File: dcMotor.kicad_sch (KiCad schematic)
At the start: 132 parts, among them J1 USB_C_Receptacle_USB2.0_16P, J3 Conn_ST_STDC14, J6 Conn_01x02_Pin, J7 Conn_01x04_Pin, J8 Conn_01x06_Pin, Q1 AO3400A, SW1 SW_Push, SW2 SW_Push, U1 LMR54406DBVR, U10 MCP6561-OT, U11 TLV9152IDR, U12 NUCLEO-F411RE:NUCLEO-F411RE, U2 NCP718ASNADJT1G, U3 NCP718ASNADJT1G, U5 TLV9152IDR, U6 ER_OLEDM0.91_1x-I2C, U7 STM32G431CBTx, U8 LTH-301-05, U9 DRV8231ADDA

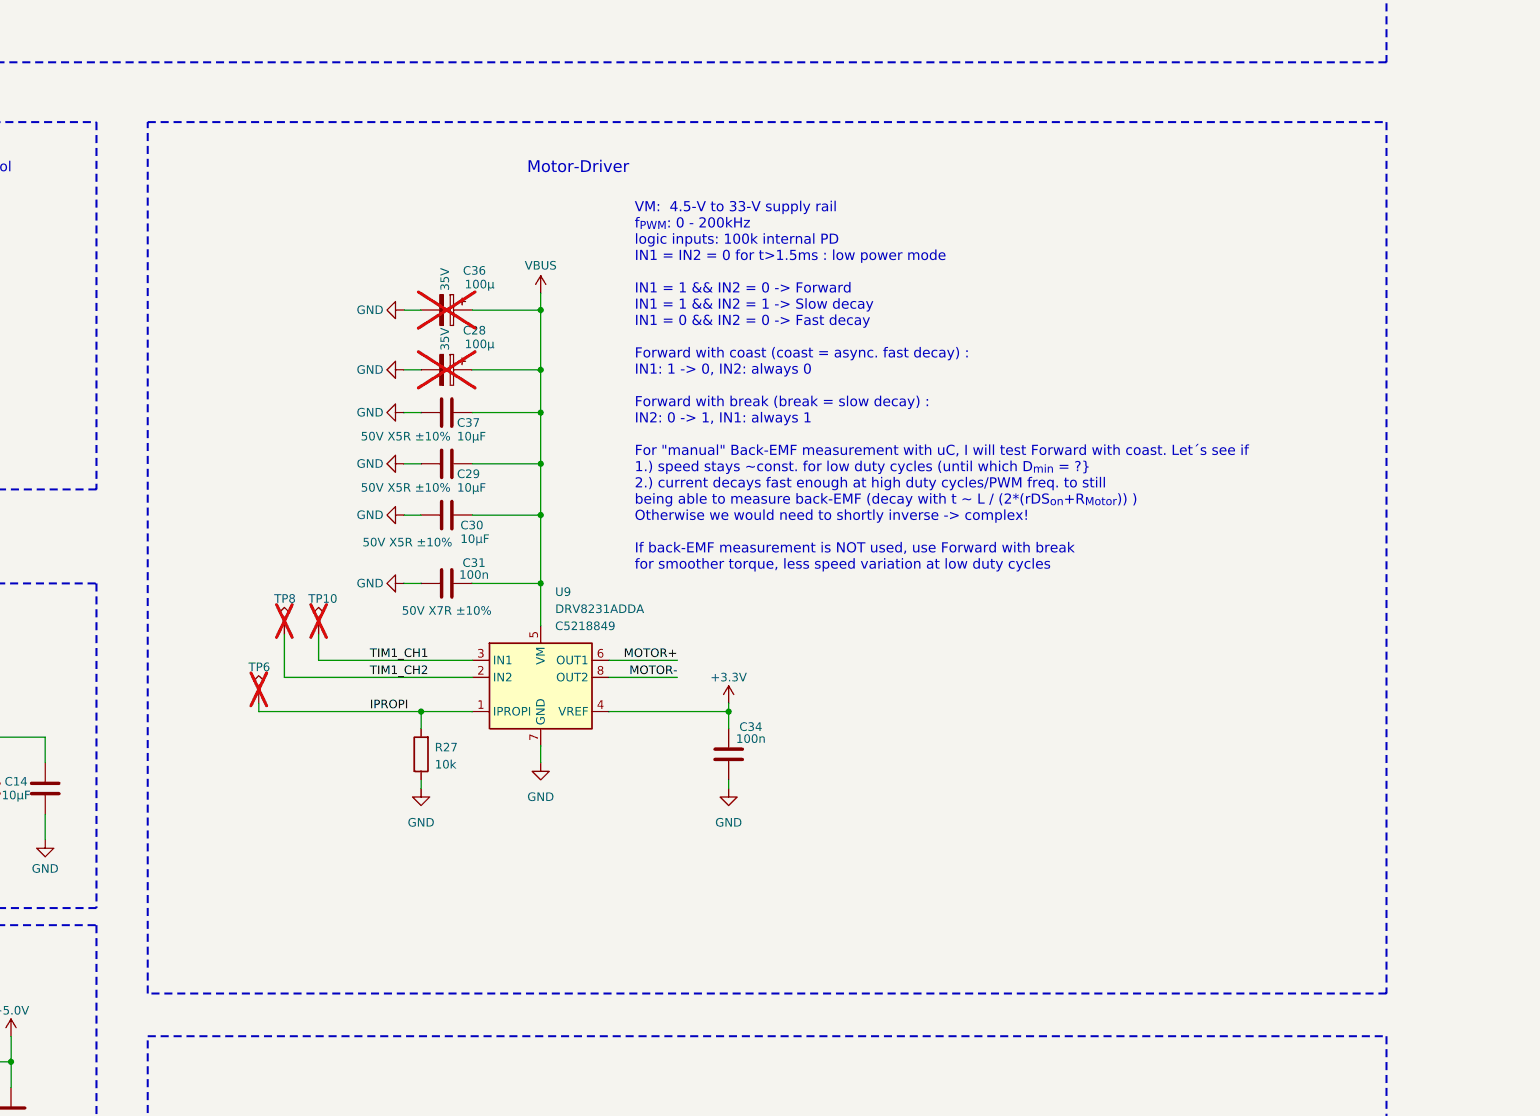
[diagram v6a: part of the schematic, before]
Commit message: added filter caps on pwm inputs because of DRV8321 errata (glitches)
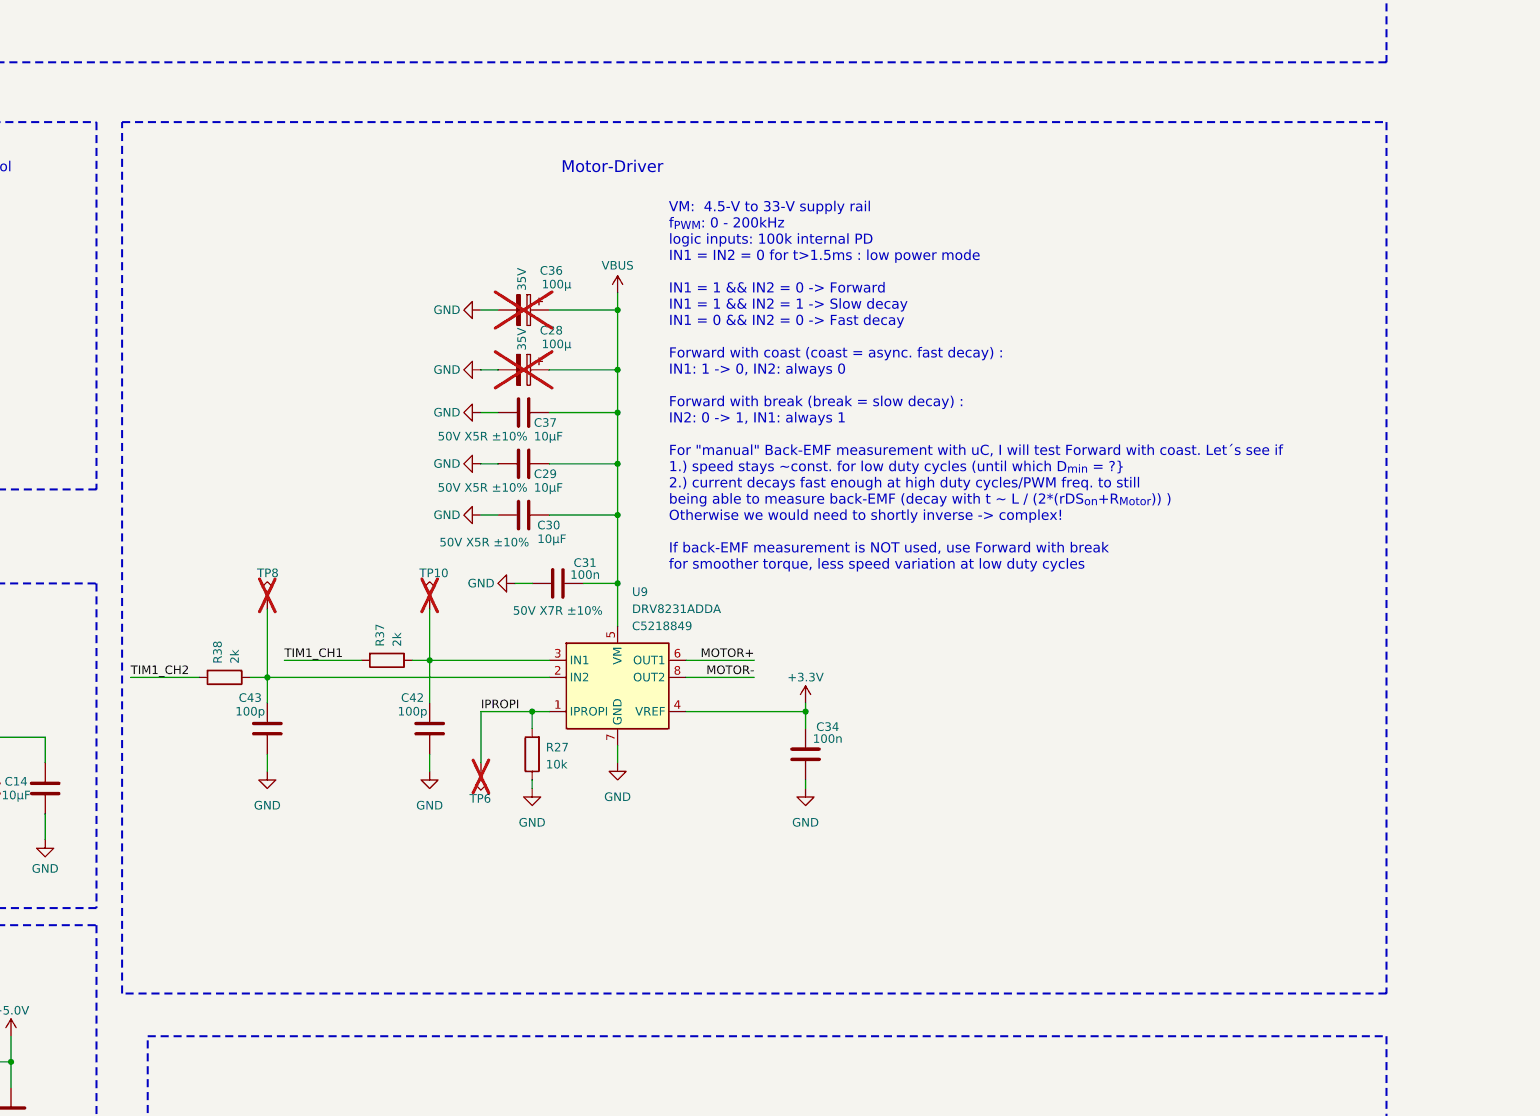
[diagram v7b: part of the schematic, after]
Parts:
- added C42, C43: 100p, Capacitor_SMD:C_0805_2012Metric_Pad1.18x1.45mm_HandSolder, symbol Device:C
- added R37, R38: 2k, Resistor_SMD:R_0805_2012Metric, symbol Device:R
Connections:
- net GND: now also C42.2, C43.2
- net TIM1_CH1: now also R37.2; no longer TP10.1, U9.3 (IN1)
- net TIM1_CH2: now also R38.2; no longer TP8.1, U9.2 (IN2)
- new net: C42.1, R37.1, TP10.1, U9.3 (IN1)
- new net: C43.1, R38.1, TP8.1, U9.2 (IN2)
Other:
- moved on the sheet: C28, C29, C30, C31, C34, C36, C37, R27, TP10, TP6, TP8, U9

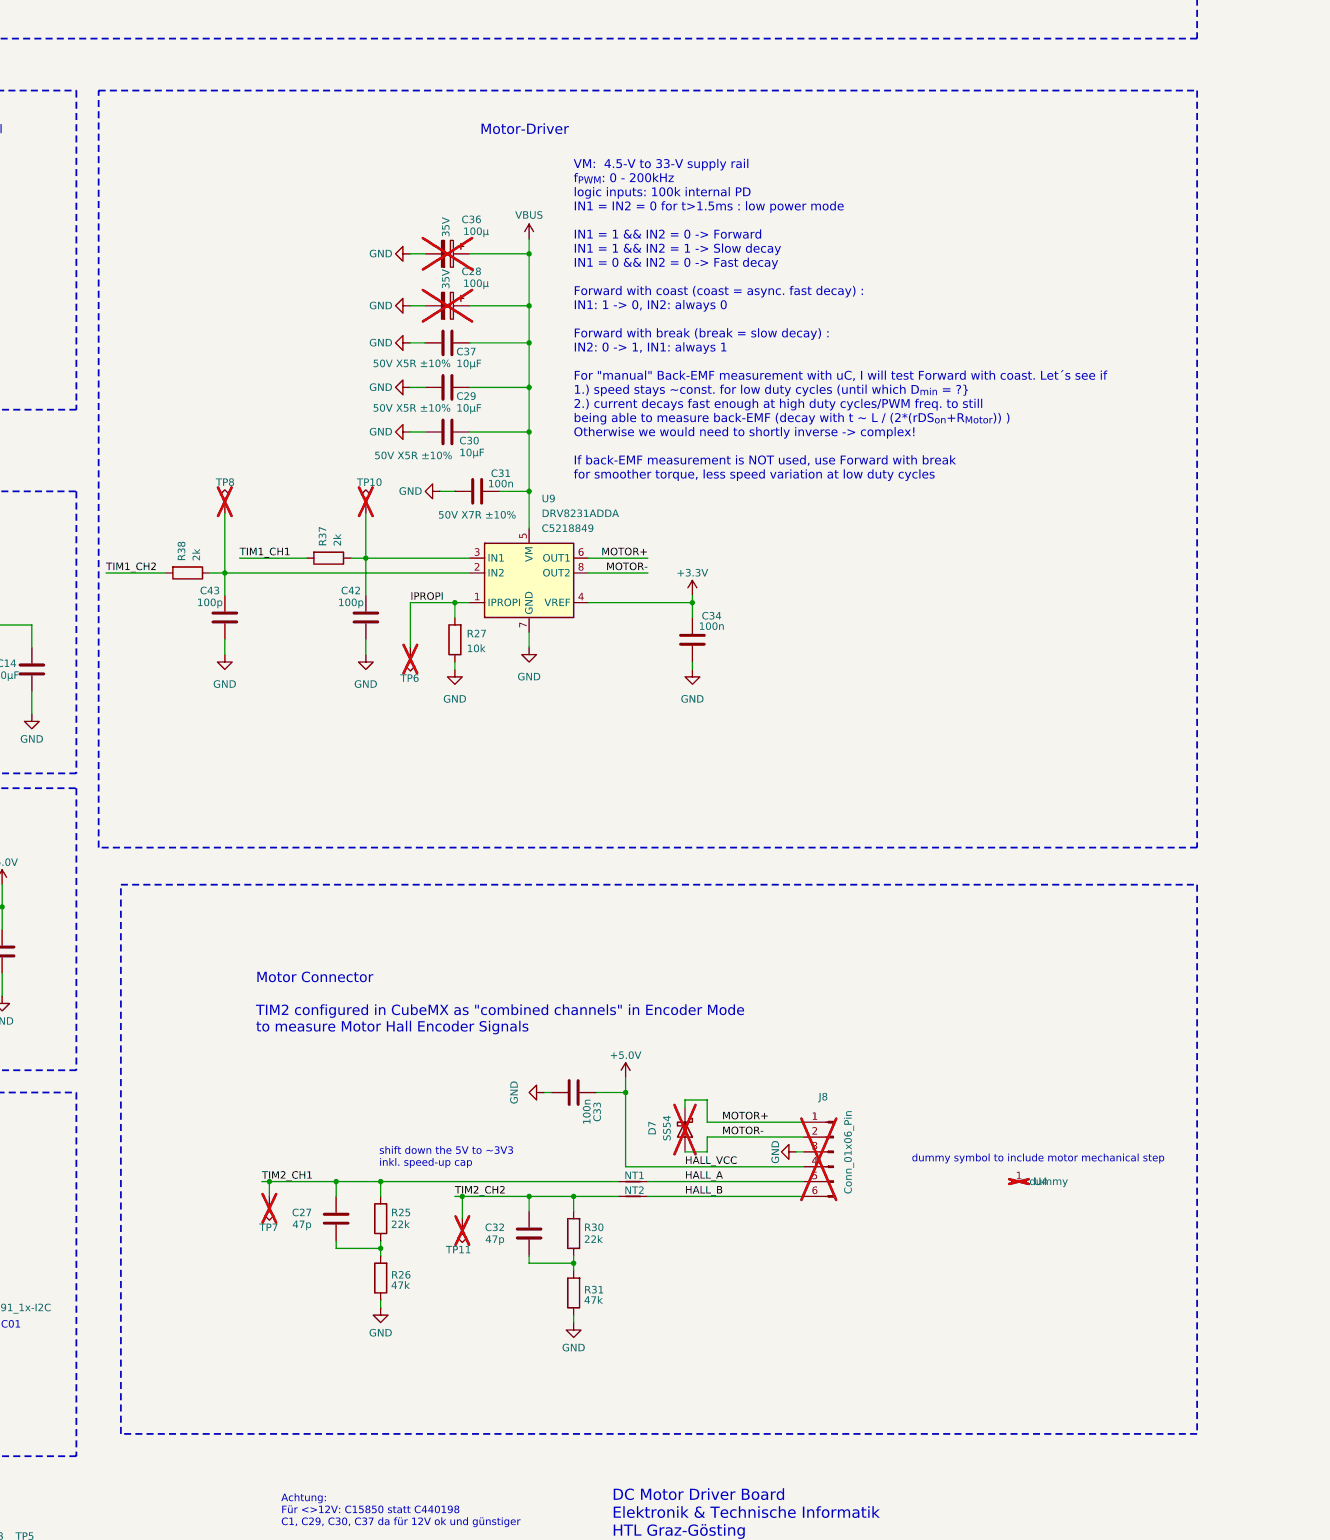
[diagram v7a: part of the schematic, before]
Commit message: wip. that is a fuc** dumb motor driver IC. thanks for nothing, TI
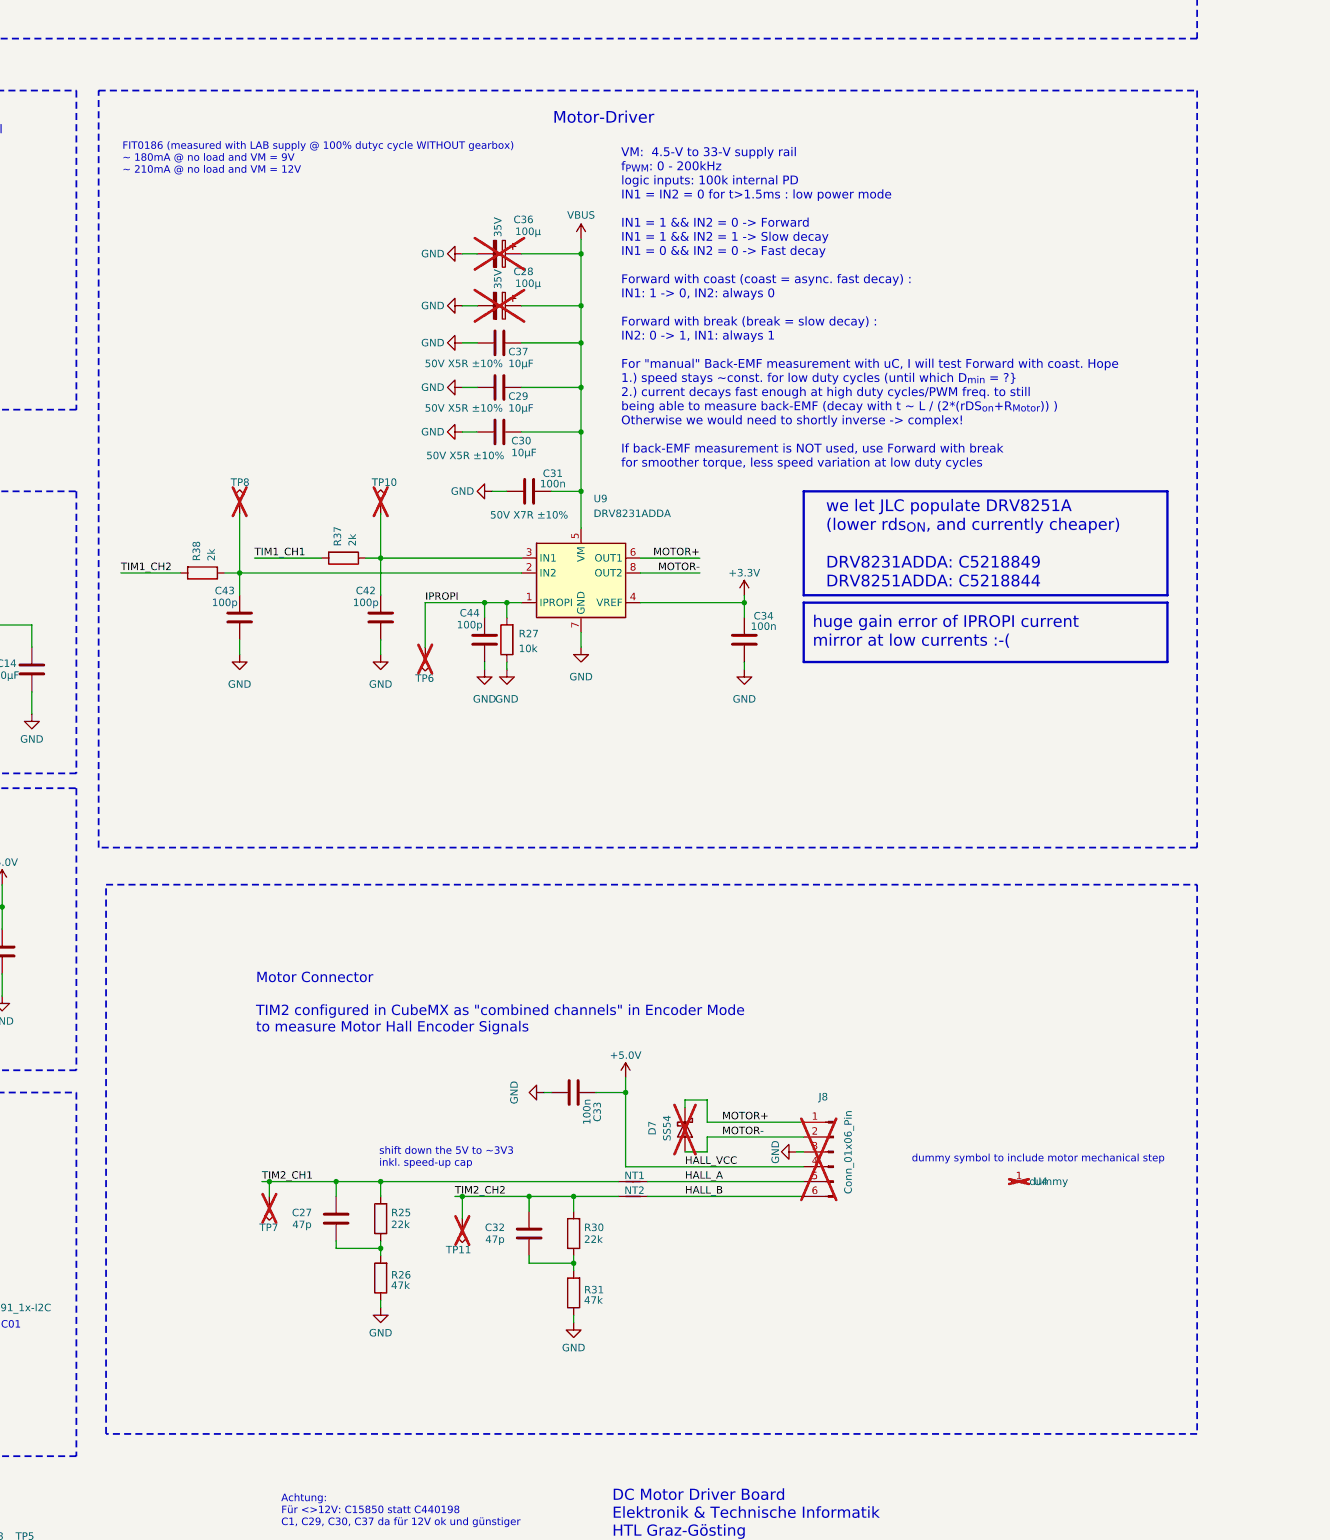
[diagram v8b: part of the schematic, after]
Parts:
- added C44: 100p, Capacitor_SMD:C_0805_2012Metric_Pad1.18x1.45mm_HandSolder, symbol Device:C
- U9: LCSC Part # C5218849 -> C5218844
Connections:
- net GND: now also C44.2
- net IPROPI: now also C44.1
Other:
- note added: "FIT0186 (measured with LAB supply @ 100% dutyc cycle WITHOUT gearbox) ~ 180mA @ no load and VM = 9V ~ 210mA @ no load and VM = 12V"
- note added: "huge gain error of IPROPI current mirror at low currents :-("
- note added: "we let JLC populate DRV8251A (lower rds_{ON}, and currently cheaper) DRV8231ADDA: C5218849 DRV8251ADDA: C5218844"
- moved on the sheet: C28, C29, C30, C31, C34, C36, C37, C42, C43, R27, R37, R38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
